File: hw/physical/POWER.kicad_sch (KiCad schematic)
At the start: 4 parts, among them U6 TPS62746, U7 TPS63030DSK

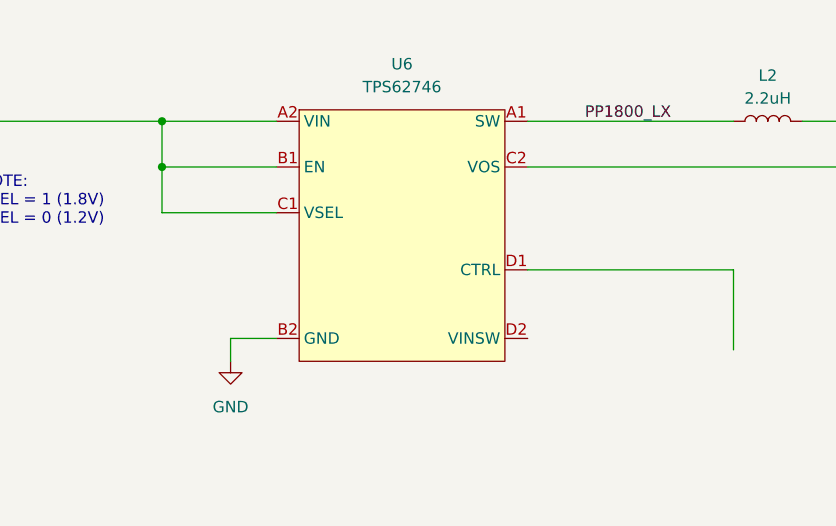
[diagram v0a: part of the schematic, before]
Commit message: Removed sch subdirectory.
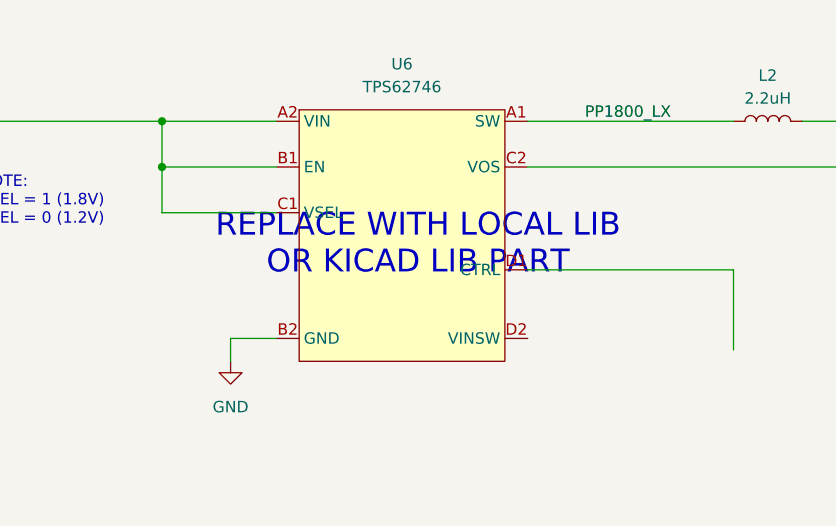
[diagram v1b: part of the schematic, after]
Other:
- note added: "REPLACE WITH LOCAL LIB OR KICAD LIB PART"
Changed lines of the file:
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@@
+		)
+	)
+	(text "REPLACE WITH LOCAL LIB \nOR KICAD LIB PART"
+		(exclude_from_sim no)
+		(at 206.248 77.216 0)
+		(effects
+			(font
+				(size 2.54 2.54)
+				(color 255 21 0 1)
+			)
 		)
 	)

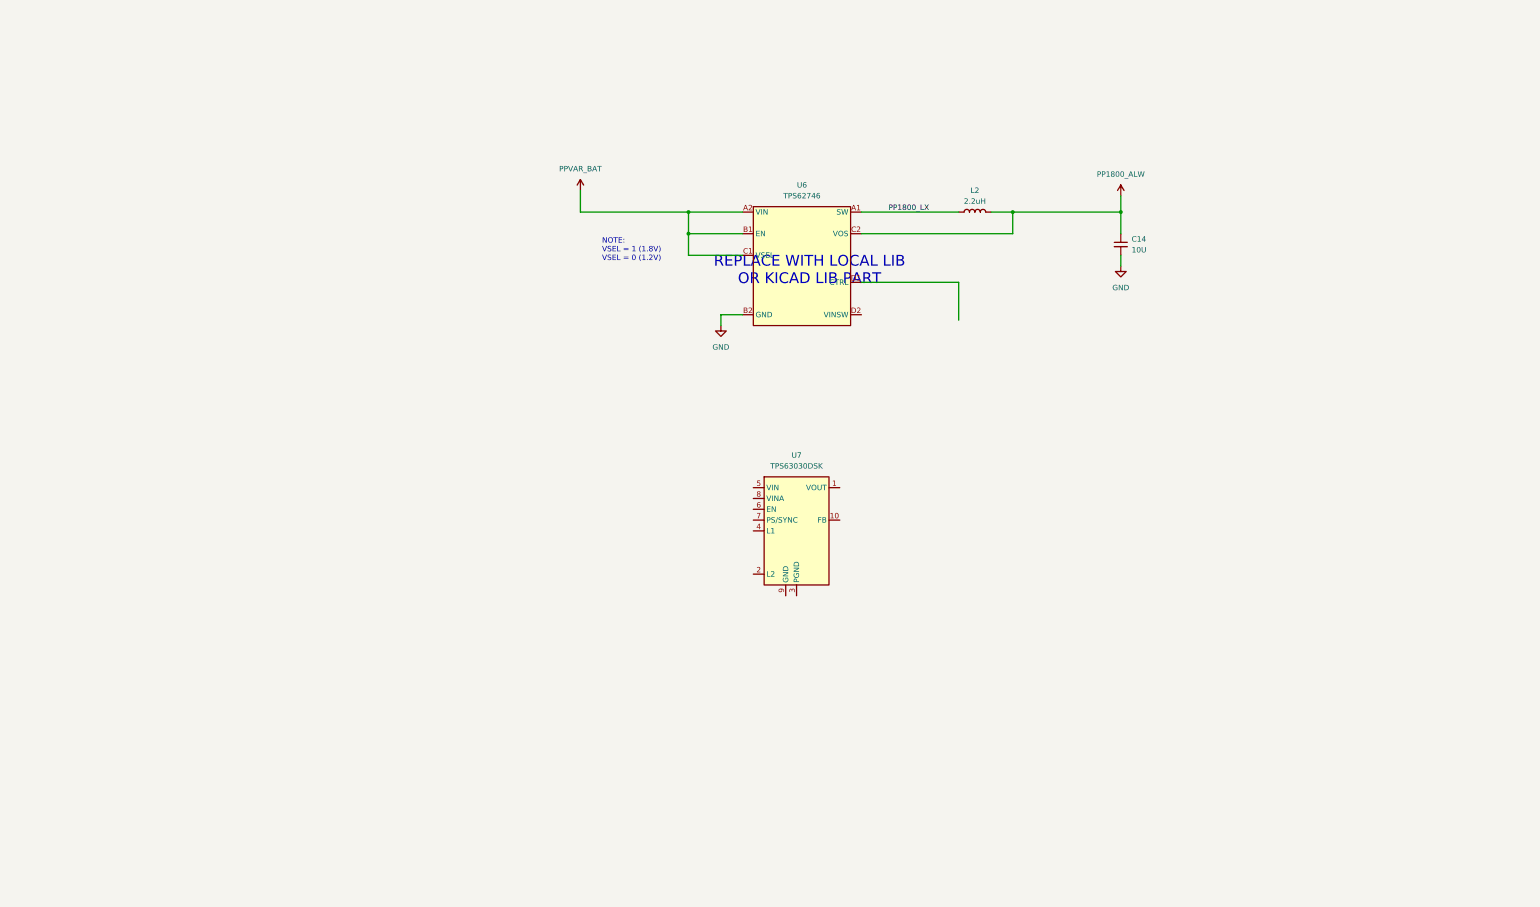
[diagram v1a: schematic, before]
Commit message: - Consolidate POWER and BATTERY pages - Updated 1.8V SYS REG to low Iq option - Replaced LoRA module with SemTech transceiver - Adding latest nRF datasheet
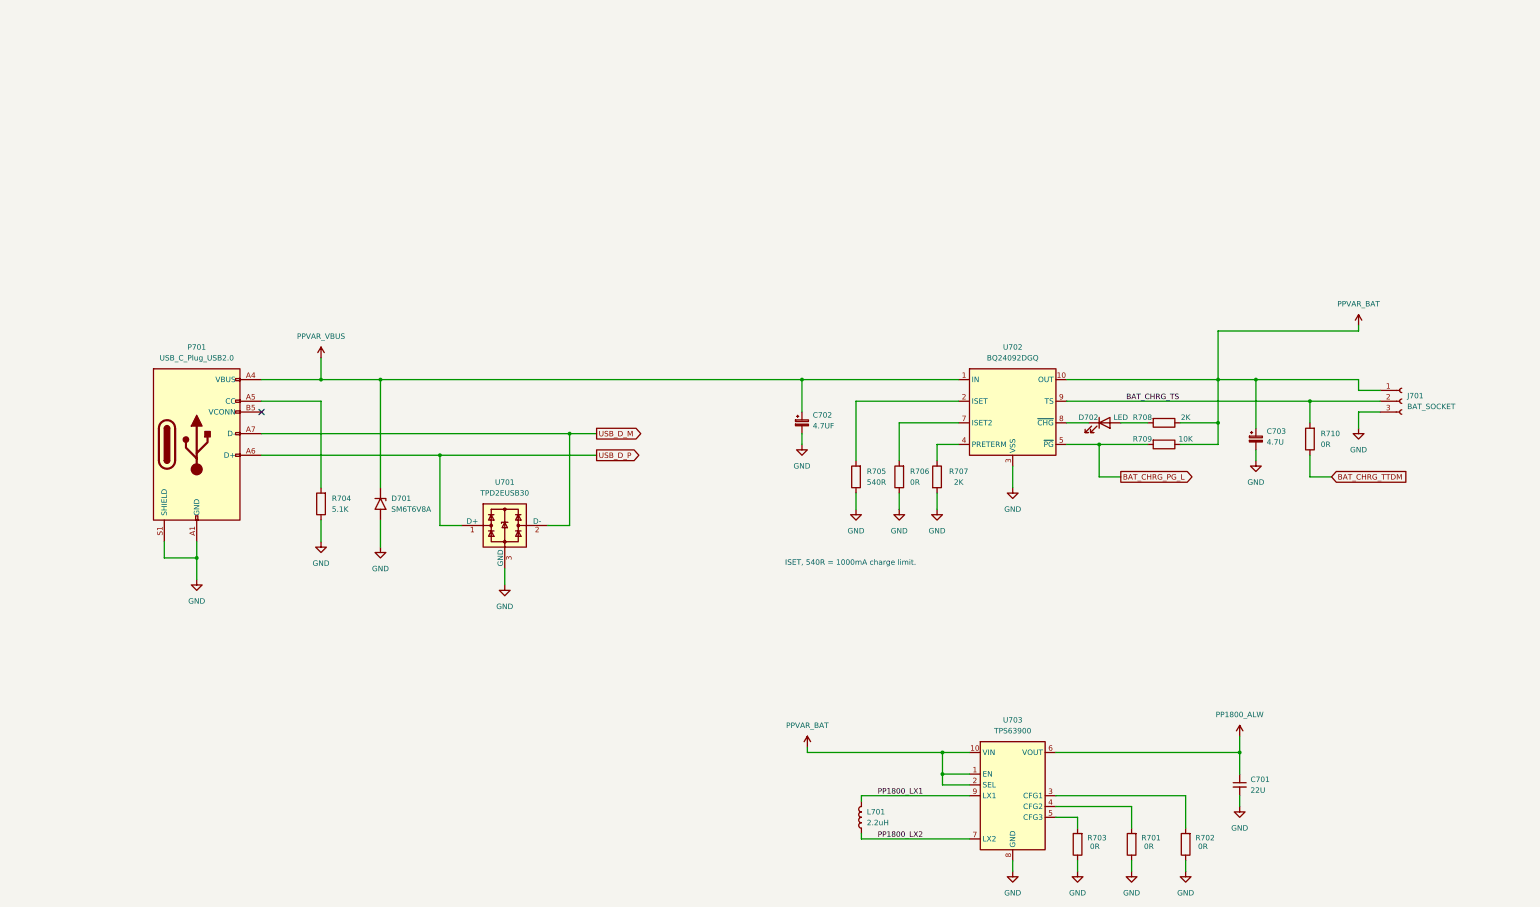
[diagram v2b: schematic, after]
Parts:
- removed C14: 10U, symbol Device:C_Small
- removed L2: 2.2uH, symbol Device:L
- removed U6: TPS62746, Package_BGA:Texas_DSBGA-8_0.705x1.468mm_Layout2x4_P0.4mm, symbol user_regulator:TPS62746
- removed U7: TPS63030DSK, Package_SON:WSON-10-1EP_2.5x2.5mm_P0.5mm_EP1.2x2mm, symbol Regulator_Switching:TPS63030DSK
- added C701: 22U, symbol Device:C_Small
- added C702: 4.7UF, symbol Device:C_Polarized_Small
- added C703: 4.7U, symbol Device:C_Polarized_Small
- added D701: SM6T6V8A, Diode_SMD:D_SMB, symbol Diode:SM6T6V8A
- added D702: LED, symbol Device:LED
- added J701: BAT_SOCKET, symbol Connector:Conn_01x03_Socket
- added L701: 2.2uH, symbol Device:L
- added P701: USB_C_Plug_USB2.0, symbol Connector:USB_C_Plug_USB2.0
- added R701, R702, R703, R706, R710: 0R, symbol Device:R
- added R704: 5.1K, symbol Device:R
- added R705: 540R, symbol Device:R
- added R707, R708: 2K, symbol Device:R
- added R709: 10K, symbol Device:R
- added U701: TPD2EUSB30, Package_TO_SOT_SMD:Texas_DRT-3, symbol Power_Protection:TPD2EUSB30
- added U702: BQ24092DGQ, Package_SO:HVSSOP-10-1EP_3x3mm_P0.5mm_EP1.57x1.88mm_ThermalVias, symbol Battery_Management:BQ24090DGQ
- added U703: TPS63900, Package_SON:WSON-10-1EP_2.5x2.5mm_P0.5mm_EP1.2x2mm_ThermalVias, symbol Regulator_Switching:TPS63900
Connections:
- net GND: now also C701.2, C702.2, C703.2, D701.2 (A2), J701.3 (Pin_3), P701.A1 (GND), P701.A12 (GND), P701.B1 (GND), P701.B12 (GND), P701.S1 (SHIELD), R701.1, R702.1, R703.1, R704.1, R705.1, R706.1, R707.2, U701.3 (GND), U702.11 (VSS), U702.3 (VSS), U703.11 (GND), U703.8 (GND)
- net PP1800_ALW: now also C701.1, U703.6 (VOUT)
- net PPVAR_BAT: now also C703.1, J701.1 (Pin_1), R708.1, R709.1, U702.10 (OUT), U703.1 (EN), U703.10 (VIN), U703.2 (SEL)
- new net: R702.2, U703.3 (CFG1)
- new net: R701.2, U703.4 (CFG2)
- new net: R703.2, U703.5 (CFG3)
- new net: R706.2, U702.7 (ISET2)
- new net: R705.2, U702.2 (ISET)
- new net: R707.1, U702.4 (PRETERM)
- new net: D702.1 (K), U702.8 (~{CHG})
- new net: D702.2 (A), R708.2
- new net: P701.A5 (CC), R704.2
- new net BAT_CHRG_PG_L: R709.2, U702.5 (~{PG})
- new net BAT_CHRG_TS: J701.2 (Pin_2), R710.2, U702.9 (TS)
- new net BAT_CHRG_TTDM: R710.1
- new net PP1800_LX1: L701.2, U703.9 (LX1)
- new net PP1800_LX2: L701.1, U703.7 (LX2)
- new net PPVAR_VBUS: C702.1, D701.1 (A1), P701.A4 (VBUS), P701.A9 (VBUS), P701.B4 (VBUS), P701.B9 (VBUS), U702.1 (IN)
- new net USB_D_M: P701.A7 (D-), U701.2 (D-)
- new net USB_D_P: P701.A6 (D+), U701.1 (D+)
- no-connect marks 0 -> 1
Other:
- note added: "ISET, 540R = 1000mA charge limit."
- note removed: "NOTE: VSEL = 1 (1.8V) VSEL = 0 (1.2V)"
- note removed: "REPLACE WITH LOCAL LIB OR KICAD LIB PART"

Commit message: Adding nRF54L10 schematic library component. Redrew MCU page with nRF54L10 and rearranged or changed net labels and global labels.
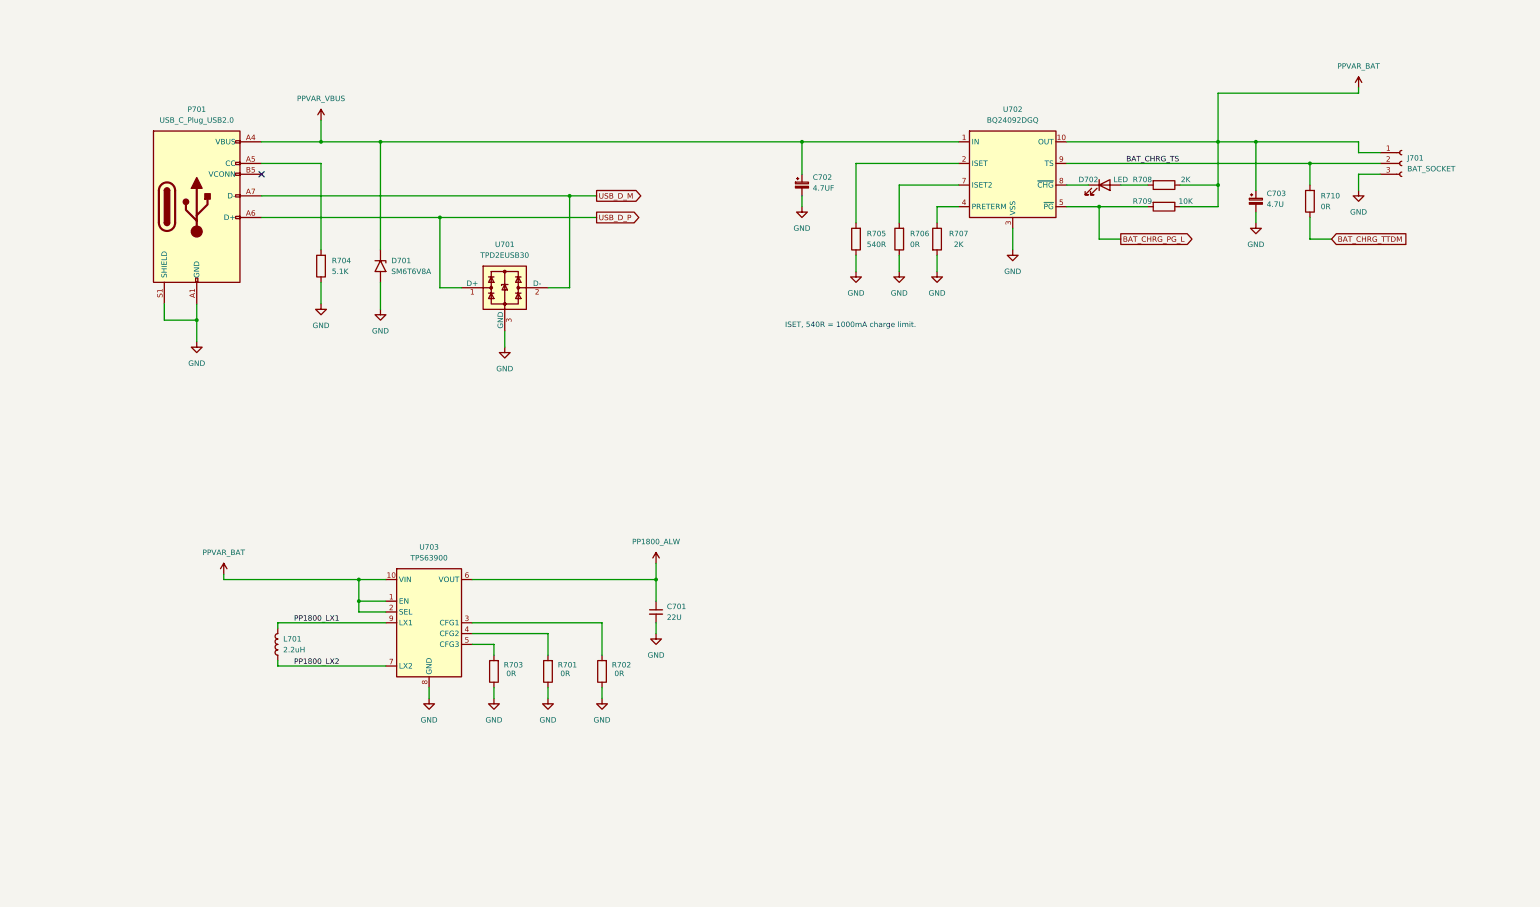
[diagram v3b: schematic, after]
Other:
- moved on the sheet: C701, C702, C703, D701, D702, J701, L701, P701, R701, R702, R703, R704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

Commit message: Various Schematic Modifications and Additions. * Removed Bypass page and moved bypass caps to MCU page. * Moved MCU VSS_PA pin to logical location as per Nordic guidelines. * Added Display Circuit, level shifters, charge pump, connector, etc. * Added 3.3V display VREG with Enable GPIO. * Added BLE RF components as per Nordic guidelines. * Added DCC circuit as per Nordic guidelines. * Rearranged GPIO's and interfaces. * Fixed various schematic errors.
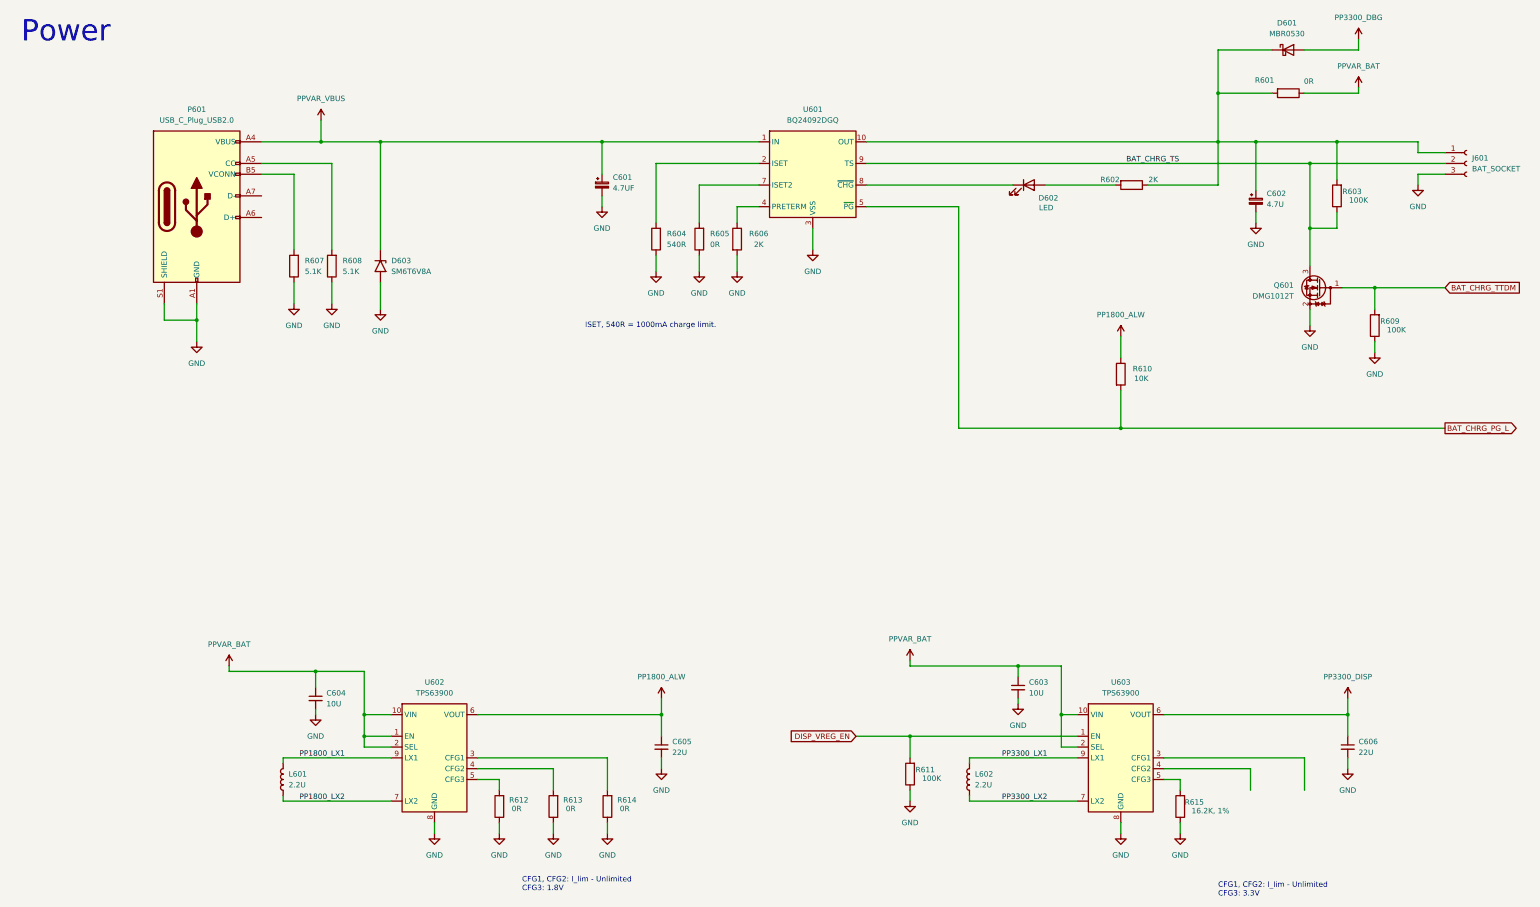
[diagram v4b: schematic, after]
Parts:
- removed R710: 0R, symbol Device:R
- removed U701: TPD2EUSB30, Package_TO_SOT_SMD:Texas_DRT-3, symbol Power_Protection:TPD2EUSB30
- added C603, C604: 10U, symbol Device:C_Small
- added C606: 22U, symbol Device:C_Small
- added D601: MBR0530, Diode_SMD:D_SOD-123, symbol Diode:MBR0530
- added L602: 2.2U, symbol Device:L
- added Q601: DMG1012T, Package_TO_SOT_SMD:SOT-523, symbol Transistor_FET:DMG1012T
- added R601: 0R, symbol Device:R
- added R603, R609, R611: 100K, symbol Device:R
- added R607: 5.1K, symbol Device:R
- added R615: 16.2K, 1%, symbol Device:R
- added U603: TPS63900, Package_SON:WSON-10-1EP_2.5x2.5mm_P0.5mm_EP1.2x2mm_ThermalVias, symbol Regulator_Switching:TPS63900
- L601: renamed from L701; value 2.2uH -> 2.2U
- renumbered C702 to C601, C703 to C602, C701 to C605, D702 to D602, D701 to D603, J701 to J601, P701 to P601, R708 to R602, R705 to R604, R706 to R605, R707 to R606, R704 to R608, R709 to R610, R703 to R612, R701 to R613, R702 to R614, U702 to U601, U703 to U602
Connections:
- net BAT_CHRG_TS: now also Q601.3 (D), R603.1
- net BAT_CHRG_TTDM: now also Q601.1 (G), R609.2
- net GND: now also C603.2, C604.2, C606.2, Q601.2 (S), R607.1, R609.1, R611.1, R615.1, U603.11 (GND), U603.8 (GND)
- net PP1800_ALW: now also R610.1
- net PPVAR_BAT: now also C603.1, C604.1, R601.1, U603.10 (VIN), U603.2 (SEL); no longer C602.1, J601.1 (Pin_1), R602.1, R610.1, U601.10 (OUT)
- net at P601.B5 (VCONN): now also R607.2
- net USB_D_M: no longer names the net of P601.A7 (D-)
- net USB_D_P: no longer names the net of P601.A6 (D+)
- new net: C602.1, D601.1 (K), J601.1 (Pin_1), R601.2, R602.1, R603.2, U601.10 (OUT)
- new net: R615.2, U603.5 (CFG3)
- new net DISP_VREG_EN: R611.2, U603.1 (EN)
- new net PP3300_DBG: D601.2 (A)
- new net PP3300_DISP: C606.1, U603.6 (VOUT)
- new net PP3300_LX1: L602.2, U603.9 (LX1)
- new net PP3300_LX2: L602.1, U603.7 (LX2)
- no-connect marks 1 -> 0
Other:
- note added: "CFG1, CFG2: I_lim - Unlimited CFG3: 1.8V"
- note added: "CFG1, CFG2: I_lim - Unlimited CFG3: 3.3V"
- note added: "Power"
- moved on the sheet: C601, C605, D602, J601, L601, R602, R604, R605, R606, R608, R610, R612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
